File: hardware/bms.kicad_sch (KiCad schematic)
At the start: 31 parts, among them Q1 Q_NMOS_DGS, U5 MAX77751, U6 LM75B, U7 MAX17048G

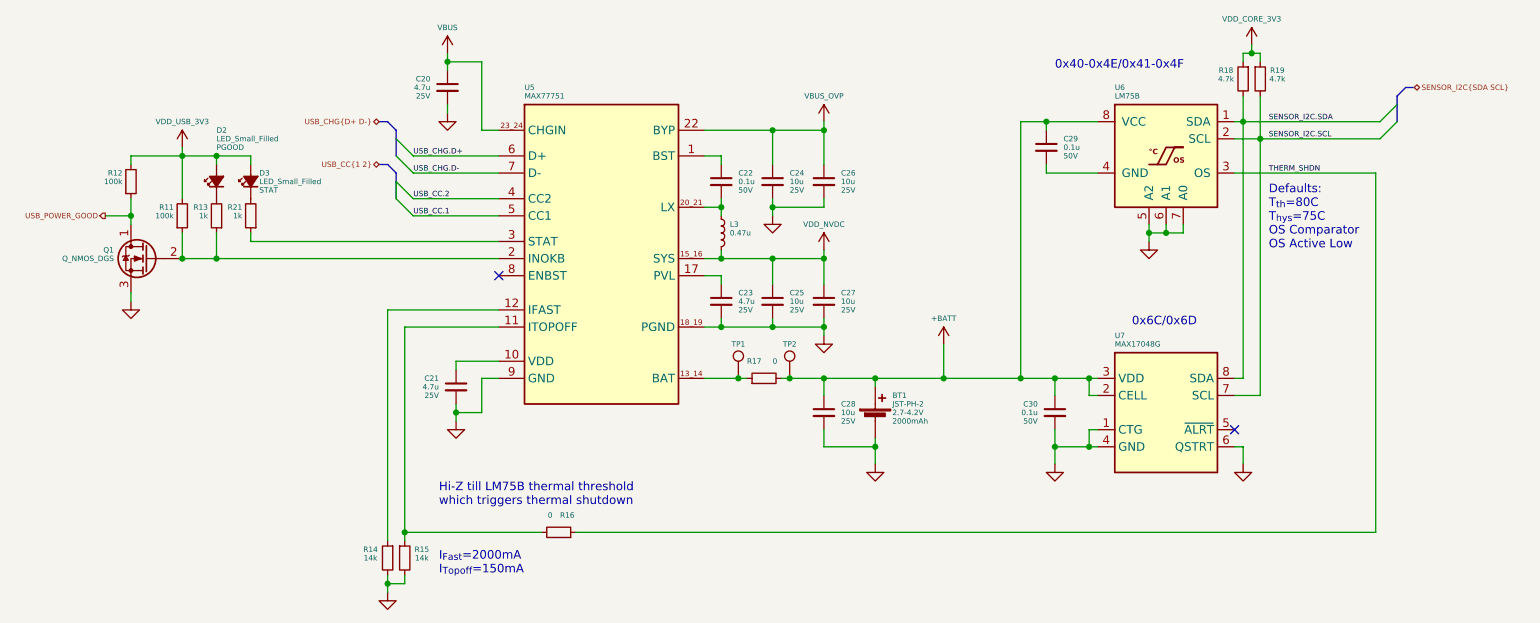
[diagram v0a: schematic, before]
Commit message: schematic tidy up, component placement, shielding investigation
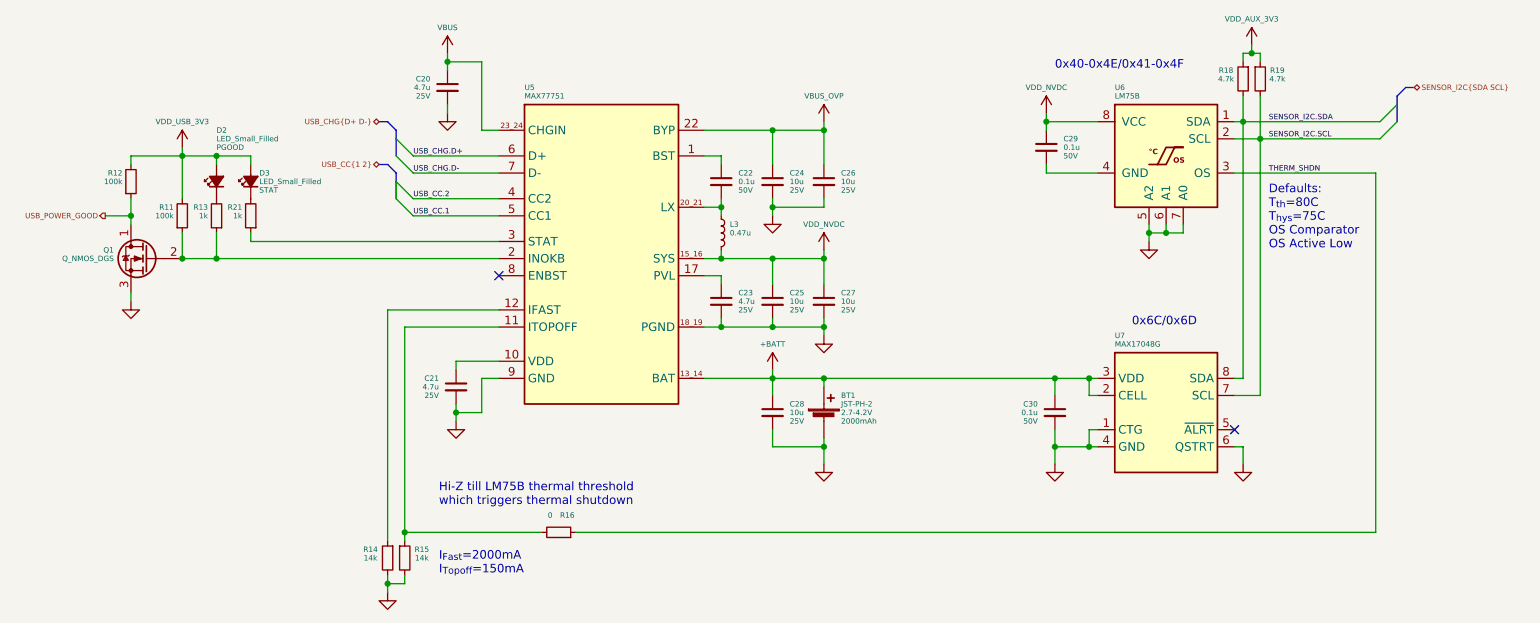
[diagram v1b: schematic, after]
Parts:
- removed R17: 0, Resistor_SMD:R_0805_2012Metric, symbol Device:R_Small
- removed TP1: SNS_BAT-, symbol Connector:TestPoint
- removed TP2: SNS_BAT+, symbol Connector:TestPoint
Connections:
- net +BATT: now also U5.13_14 (BAT); no longer C29.1, U6.8 (VCC)
- net VDD_NVDC: now also C29.1, U6.8 (VCC)
- net 3V3_CORE renamed VDD_AUX_3V3
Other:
- moved on the sheet: BT1, C28

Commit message: minor sch tweaks, more layout, added power emc shield
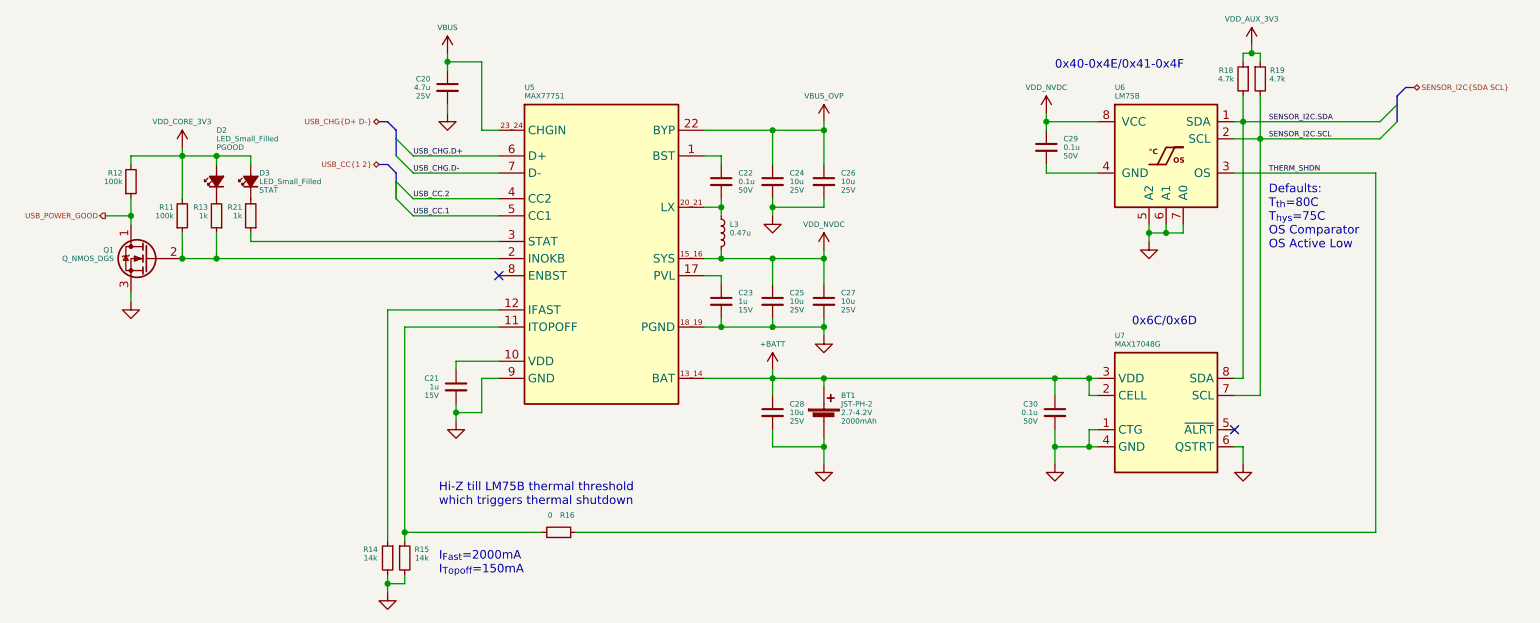
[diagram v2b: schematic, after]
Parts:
- C21, C23: value 4.7u -> 1u; footprint Capacitor_SMD:C_0603_1608Metric -> Capacitor_SMD:C_0402_1005Metric; Voltage 25V -> 15V
- C24, C25, C26, C27, C28: footprint Capacitor_SMD:C_0805_2012Metric -> Capacitor_SMD:C_0603_1608Metric
- U5: footprint Package_QFN_bt:FC2QFN-24-3x3_P0.4mm -> bt_Package_QFN:FC2QFN-24-3x3_P0.4mm
- U6: footprint Package_DFN_QFN:DFN-8-1EP_2x2mm_P0.5mm_EP0.7x1.3mm -> bt_Package_SON:XSON-8U
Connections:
- net VDD_USB_3V3 renamed VDD_CORE_3V3
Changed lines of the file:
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@@
       (effects (font (size 0.8 0.8)) (justify left))
     )
-    (property "Footprint" "Capacitor_SMD:C_0805_2012Metric" (id 2) (at 137.16 97.79 0)
+    (property "Footprint" "Capacitor_SMD:C_0603_1608Metric" (id 2) (at 137.16 97.79 0)
       (effects (font (size 0.8 0.8)) hide)
     )
@@
       (effects (font (size 0.8 0.8)) (justify left))
     )
-    (property "Footprint" "Package_QFN_bt:FC2QFN-24-3x3_P0.4mm" (id 2) (at 111.76 49.53 0)
+    (property "Footprint" "bt_Package_QFN:FC2QFN-24-3x3_P0.4mm" (id 2) (at 111.76 49.53 0)
       (effects (font (size 0.8 0.8)) hide)
     )
@@
       (effects (font (size 0.8 0.8)) (justify left))
     )
-    (property "Footprint" "Package_DFN_QFN:DFN-8-1EP_2x2mm_P0.5mm_EP0.7x1.3mm" (id 2) (at 195.58 58.42 0)
+    (property "Footprint" "bt_Package_SON:XSON-8U" (id 2) (at 195.58 58.42 0)
       (effects (font (size 0.8 0.8)) hide)
     )
@@
       (effects (font (size 0.8 0.8)) (justify left))
     )
-    (property "Footprint" "Capacitor_SMD:C_0805_2012Metric" (id 2) (at 137.16 63.5 0)
+    (property "Footprint" "Capacitor_SMD:C_0603_1608Metric" (id 2) (at 137.16 63.5 0)
       (effects (font (size 0.8 0.8)) hide)
     )
@@
       (effects (font (size 0.8 0.8)) (justify left))
     )
-    (property "Footprint" "Capacitor_SMD:C_0805_2012Metric" (id 2) (at 137.16 81.28 0)
+    (property "Footprint" "Capacitor_SMD:C_0603_1608Metric" (id 2) (at 137.16 81.28 0)
       (effects (font (size 0.8 0.8)) hide)
     )
@@
     (pin "2")
   )
-  (symbol (lib_id "bt_power:VDD_USB_3V3") (at 49.53 58.42 0) (unit 1)
-    (in_bom no) (on_board no)
-    (property "Reference" "#U0102" (id 0) (at 50.0634 58.42 0)
-      (effects (font (size 1.27 1.27)) hide)
-    )
-    (property "Value" "VDD_USB_3V3" (id 1) (at 49.53 54.61 0)
-      (effects (font (size 0.8 0.8)))
-    )
-    (property "Footprint" "" (id 2) (at 50.0634 58.42 0)
-      (effects (font (size 1.27 1.27)) hide)
-    )
-    (property "Datasheet" "" (id 3) (at 50.0634 58.42 0)
-      (effects (font (size 1.27 1.27)) hide)
-    )
-    (pin "1")
-  )
   (symbol (lib_id "Device:C_Small") (at 129.54 63.5 0) (unit 1)
     (in_bom yes) (on_board yes)
@@
     (pin "2")
   )
-  (symbol (lib_id "Device:C_Small") (at 90.17 93.98 0) (mirror y) (unit 1)
-    (in_bom yes) (on_board yes)
-    (property "Reference" "C21" (id 0) (at 87.63 92.71 0)
-      (effects (font (size 0.8 0.8)) (justify left))
-    )
-    (property "Value" "4.7u" (id 1) (at 87.63 93.98 0)
-      (effects (font (size 0.8 0.8)) (justify left))
-    )
-    (property "Footprint" "Capacitor_SMD:C_0603_1608Metric" (id 2) (at 90.17 93.98 0)
-      (effects (font (size 0.8 0.8)) hide)
-    )
-    (property "Datasheet" "~" (id 3) (at 90.17 93.98 0)
-      (effects (font (size 0.8 0.8)) hide)
-    )
-    (property "Voltage" "25V" (id 4) (at 87.63 95.25 0)
-      (effects (font (size 0.8 0.8)) (justify left))
-    )
-    (pin "1")
-    (pin "2")
-  )
   (symbol (lib_id "power:GND") (at 41.91 81.28 0) (mirror y) (unit 1)
     (in_bom yes) (on_board yes)
@@
     (property "Datasheet" "~" (id 3) (at 209.55 48.26 0)
       (effects (font (size 0.8 0.8)) hide)
-    )
-    (pin "1")
-    (pin "2")
-  )
-  (symbol (lib_id "Device:C_Small") (at 129.54 81.28 0) (unit 1)
-    (in_bom yes) (on_board yes)
-    (property "Reference" "C23" (id 0) (at 132.08 80.01 0)
-      (effects (font (size 0.8 0.8)) (justify left))
-    )
-    (property "Value" "4.7u" (id 1) (at 132.08 81.28 0)
-      (effects (font (size 0.8 0.8)) (justify left))
-    )
-    (property "Footprint" "Capacitor_SMD:C_0603_1608Metric" (id 2) (at 129.54 81.28 0)
-      (effects (font (size 0.8 0.8)) hide)
-    )
-    (property "Datasheet" "~" (id 3) (at 129.54 81.28 0)
-      (effects (font (size 0.8 0.8)) hide)
-    )
-    (property "Voltage" "25V" (id 4) (at 132.08 82.55 0)
-      (effects (font (size 0.8 0.8)) (justify left))
     )
     (pin "1")
@@
     (pin "8")
   )
+  (symbol (lib_id "Device:C_Small") (at 129.54 81.28 0) (unit 1)
+    (in_bom yes) (on_board yes)
+    (property "Reference" "C23" (id 0) (at 132.08 80.01 0)
+      (effects (font (size 0.8 0.8)) (justify left))
+    )
+    (property "Value" "1u" (id 1) (at 132.08 81.28 0)
+      (effects (font (size 0.8 0.8)) (justify left))
+    )
+    (property "Footprint" "Capacitor_SMD:C_0402_1005Metric" (id 2) (at 129.54 81.28 0)
+      (effects (font (size 0.8 0.8)) hide)
+    )
+    (property "Datasheet" "~" (id 3) (at 129.54 81.28 0)
+      (effects (font (size 0.8 0.8)) hide)
+    )
+    (property "Voltage" "15V" (id 4) (at 132.08 82.55 0)
+      (effects (font (size 0.8 0.8)) (justify left))
+    )
+    (pin "1")
+    (pin "2")
+  )
   (symbol (lib_id "bt_power:VDD_NVDC") (at 144.78 73.66 0) (unit 1)
     (in_bom no) (on_board no)
@@
       (effects (font (size 0.8 0.8)) (justify left))
     )
-    (property "Footprint" "Capacitor_SMD:C_0805_2012Metric" (id 2) (at 144.78 63.5 0)
+    (property "Footprint" "Capacitor_SMD:C_0603_1608Metric" (id 2) (at 144.78 63.5 0)
       (effects (font (size 0.8 0.8)) hide)
     )
@@
       (effects (font (size 0.8 0.8)) (justify left))
     )
-    (property "Footprint" "Capacitor_SMD:C_0805_2012Metric" (id 2) (at 144.78 81.28 0)
+    (property "Footprint" "Capacitor_SMD:C_0603_1608Metric" (id 2) (at 144.78 81.28 0)
       (effects (font (size 0.8 0.8)) hide)
     )
@@
     (pin "2")
   )
+  (symbol (lib_id "bt_power:VDD_CORE_3V3") (at 49.53 58.42 0) (unit 1)
+    (in_bom no) (on_board no)
+    (property "Reference" "#U0102" (id 0) (at 50.0634 58.42 0)
+      (effects (font (size 1.27 1.27)) hide)
+    )
+    (property "Value" "VDD_CORE_3V3" (id 1) (at 45.085 54.61 0)
+      (effects (font (size 0.8 0.8)) (justify left))
+    )
+    (property "Footprint" "" (id 2) (at 50.0634 58.42 0)
+      (effects (font (size 1.27 1.27)) hide)
+    )
+    (property "Datasheet" "" (id 3) (at 50.0634 58.42 0)
+      (effects (font (size 1.27 1.27)) hide)
+    )
+    (pin "1")
+  )
   (symbol (lib_id "power:GND") (at 80.01 124.46 0) (unit 1)
     (in_bom yes) (on_board yes) (fields_autoplaced)
@@
       (effects (font (size 0.8 0.8)) (justify left))
     )
+    (pin "1")
+    (pin "2")
+  )
+  (symbol (lib_id "Device:C_Small") (at 90.17 93.98 0) (mirror y) (unit 1)
+    (in_bom yes) (on_board yes)
+    (property "Reference" "C21" (id 0) (at 87.63 92.71 0)
+      (effects (font (size 0.8 0.8)) (justify left))
+    )
+    (property "Value" "1u" (id 1) (at 87.63 93.98 0)
+      (effects (font (size 0.8 0.8)) (justify left))
+    )
+    (property "Footprint" "Capacitor_SMD:C_0402_1005Metric" (id 2) (at 90.17 93.98 0)
+      (effects (font (size 0.8 0.8)) hide)
+    )
+    (property "Datasheet" "~" (id 3) (at 90.17 93.98 0)
+      (effects (font (size 0.8 0.8)) hide)
+    )
+    (property "Voltage" "15V" (id 4) (at 87.63 95.25 0)
+      (effects (font (size 0.8 0.8)) (justify left))
+    )

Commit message: screen mock, tweaked layout easier powerplane division
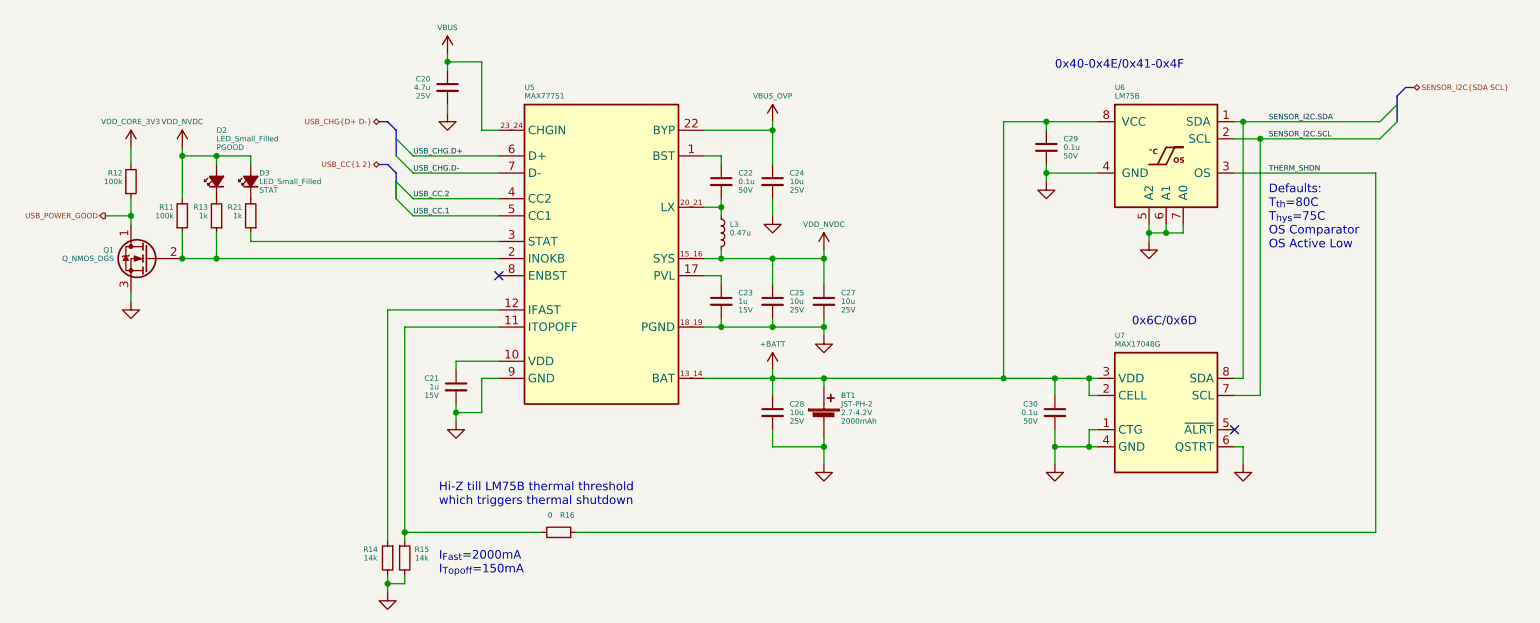
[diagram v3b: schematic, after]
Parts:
- removed C26: 10u, Capacitor_SMD:C_0603_1608Metric, symbol Device:C_Small
- removed R18, R19: 4.7k, Resistor_SMD:R_0402_1005Metric, symbol Device:R_Small
- BT1: footprint Connector_PinHeader_1.00mm:PinHeader_1x02_P1.00mm_Vertical -> Connector_PinHeader_1.27mm:PinHeader_1x02_P1.27mm_Vertical
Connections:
- net +BATT: now also C29.1, U6.8 (VCC)
- net GND: now also C29.2, U6.4 (GND)
- net VDD_CORE_3V3: no longer D2.2 (A), D3.2 (A), R11.2
- net VDD_NVDC: now also D2.2 (A), D3.2 (A), R11.2; no longer C29.1, U6.8 (VCC)

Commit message: Updates
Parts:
- D2, D3: footprint LED_SMD:LED_0603_1608Metric -> LED_SMD:LED_0402_1005Metric
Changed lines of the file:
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@@
       (effects (font (size 0.8 0.8)) (justify right))
     )
-    (property "Footprint" "LED_SMD:LED_0603_1608Metric" (id 2) (at 54.61 63.5 90)
+    (property "Footprint" "LED_SMD:LED_0402_1005Metric" (id 2) (at 54.61 63.5 90)
       (effects (font (size 1.27 1.27)) hide)
     )
@@
       (effects (font (size 0.8 0.8)) (justify right))
     )
-    (property "Footprint" "LED_SMD:LED_0603_1608Metric" (id 2) (at 59.69 63.5 90)
+    (property "Footprint" "LED_SMD:LED_0402_1005Metric" (id 2) (at 59.69 63.5 90)
       (effects (font (size 1.27 1.27)) hide)
     )
